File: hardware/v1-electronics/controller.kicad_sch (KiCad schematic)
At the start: 35 parts, among them IC1 IS31FL3733-QFLS4-TR, IC2 IS31FL3733-QFLS4-TR, J2 Conn_01x03, SW78 SW_Push, U1 MDBT50Q-1MV2

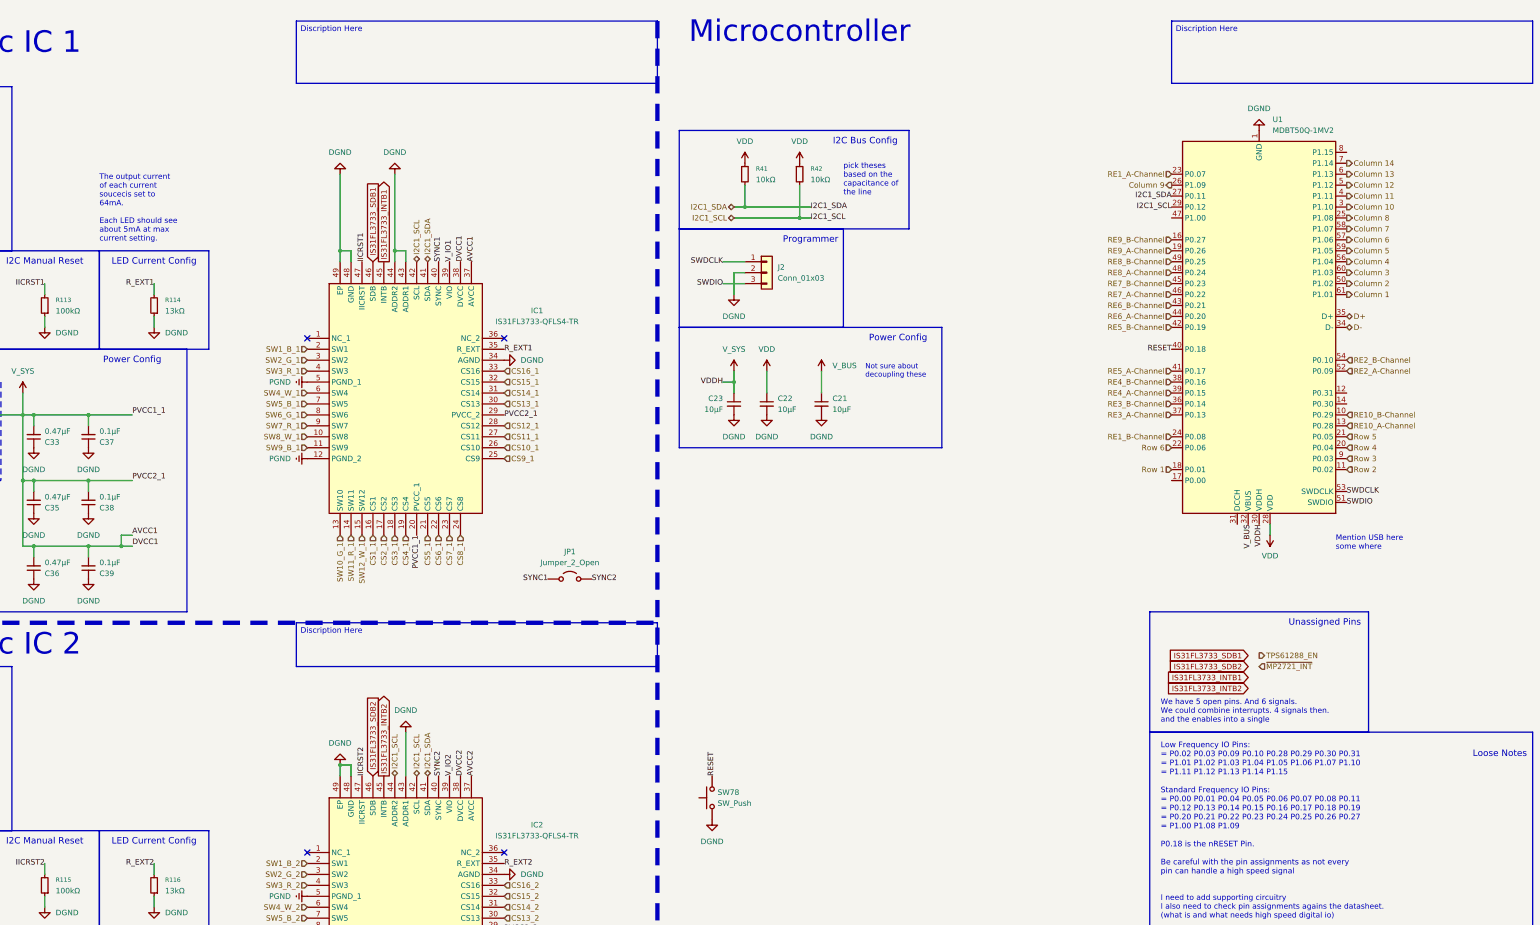
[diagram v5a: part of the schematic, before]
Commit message: refactor(v1 hardware): root level schematic is made discriptive with hierarchical pins
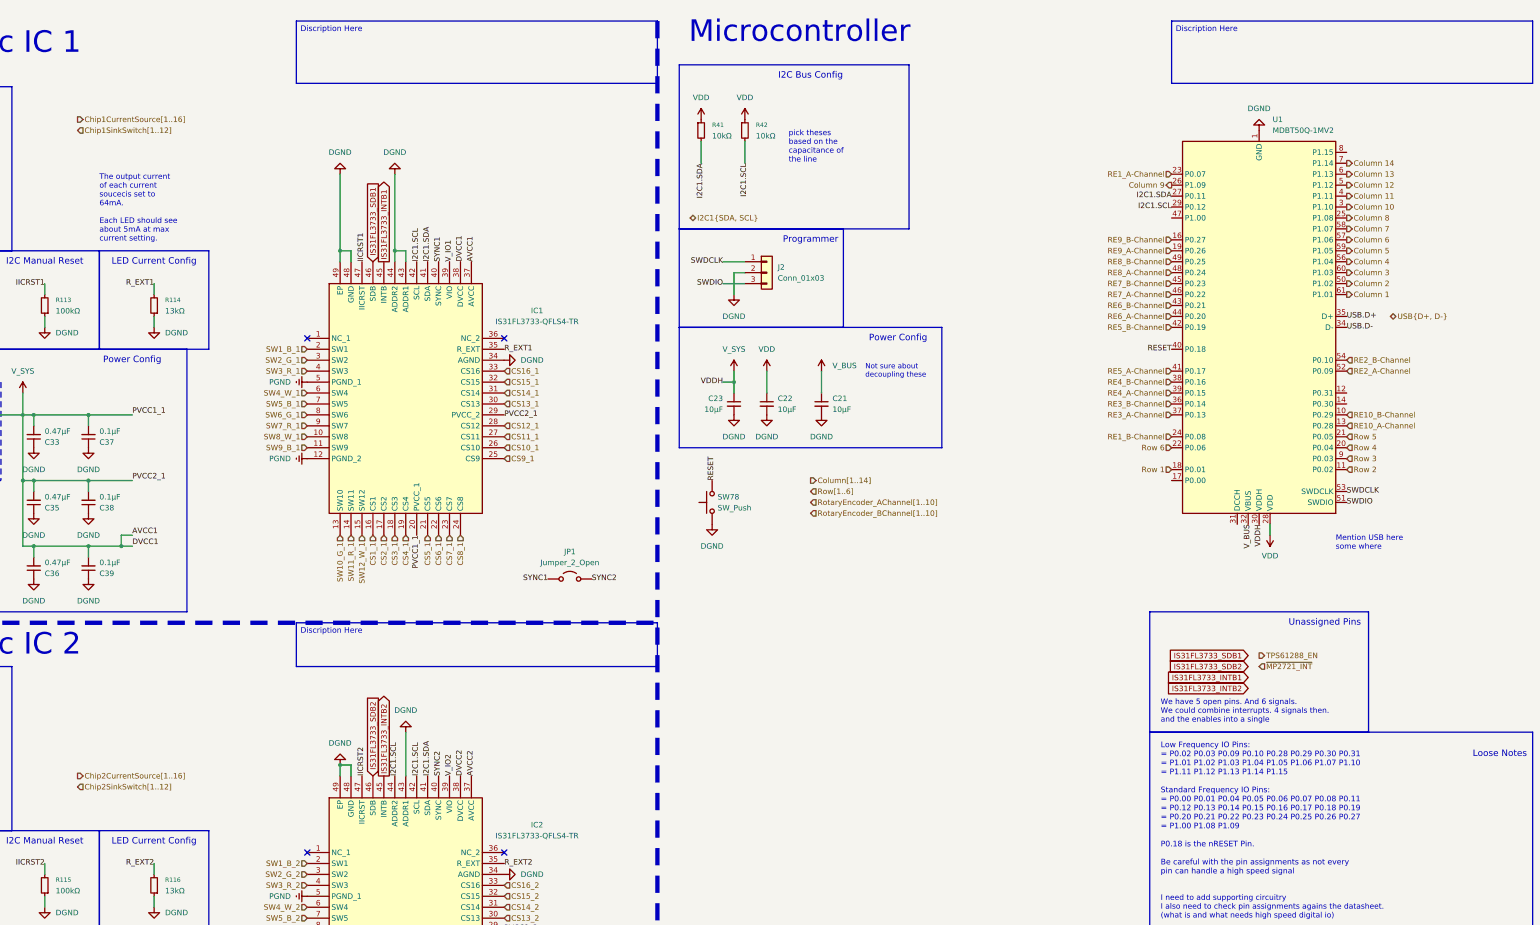
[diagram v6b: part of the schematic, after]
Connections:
- net D+ renamed USB.D+
- net D- renamed USB.D-
- net I2C1_SCL renamed I2C1.SCL
- net I2C1_SDA renamed I2C1.SDA
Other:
- moved on the sheet: R41, R42, SW78

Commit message: refactor(v1 hardware): transition to hierarchical pins complete
All the buses renamed to stuff
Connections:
- net CS10_1 renamed Chip1CurrentSource10
- net CS10_2 renamed Chip2CurrentSource10
- net CS11_1 renamed Chip1CurrentSource11
- net CS11_2 renamed Chip2CurrentSource11
- net CS12_1 renamed Chip1CurrentSource12
- net CS12_2 renamed Chip2CurrentSource12
- net CS13_1 renamed Chip1CurrentSource13
- net CS13_2 renamed Chip2CurrentSource13
- net CS14_1 renamed Chip1CurrentSource14
- net CS14_2 renamed Chip2CurrentSource14
- net CS15_1 renamed Chip1CurrentSource15
- net CS15_2 renamed Chip2CurrentSource15
- net CS16_1 renamed Chip1CurrentSource16
- net CS16_2 renamed Chip2CurrentSource16
- net CS1_1 renamed Chip1CurrentSource1
- net CS1_2 renamed Chip2CurrentSource1
- net CS2_1 renamed Chip1CurrentSource2
- net CS2_2 renamed Chip2CurrentSource2
- net CS3_1 renamed Chip1CurrentSource3
- net CS3_2 renamed Chip2CurrentSource3
- net CS4_1 renamed Chip1CurrentSource4
- net CS4_2 renamed Chip2CurrentSource4
- net CS5_1 renamed Chip1CurrentSource5
- net CS5_2 renamed Chip2CurrentSource5
- net CS6_1 renamed Chip1CurrentSource6
- net CS6_2 renamed Chip2CurrentSource6
- net CS7_1 renamed Chip1CurrentSource7
- net CS7_2 renamed Chip2CurrentSource7
- net CS8_1 renamed Chip1CurrentSource8
- net CS8_2 renamed Chip2CurrentSource8
- net CS9_1 renamed Chip1CurrentSource9
- net CS9_2 renamed Chip2CurrentSource9
- net Column 1 renamed Column1
- net Column 10 renamed Column10
- net Column 11 renamed Column11
- net Column 12 renamed Column12
- net Column 13 renamed Column13
- net Column 14 renamed Column14
- net Column 2 renamed Column2
- net Column 3 renamed Column3
- net Column 4 renamed Column4
- net Column 5 renamed Column5
- net Column 6 renamed Column6
- net Column 7 renamed Column7
- net Column 8 renamed Column8
- net Column 9 renamed Column9
- net RE10_A-Channel renamed RotaryEncoder_AChannel10
- net RE10_B-Channel renamed RotaryEncoder_BChannel10
- net RE1_A-Channel renamed RotaryEncoder_AChannel1
- net RE1_B-Channel renamed RotaryEncoder_BChannel1
- net RE2_A-Channel renamed RotaryEncoder_AChannel2
- net RE2_B-Channel renamed RotaryEncoder_BChannel2
- net RE3_A-Channel renamed RotaryEncoder_AChannel3
- net RE3_B-Channel renamed RotaryEncoder_BChannel3
- net RE4_A-Channel renamed RotaryEncoder_AChannel4
- net RE4_B-Channel renamed RotaryEncoder_BChannel4
- net RE5_A-Channel renamed RotaryEncoder_AChannel5
- net RE5_B-Channel renamed RotaryEncoder_BChannel5
- net RE6_A-Channel renamed RotaryEncoder_AChannel6
- net RE6_B-Channel renamed RotaryEncoder_BChannel6
- net RE7_A-Channel renamed RotaryEncoder_AChannel7
- net RE7_B-Channel renamed RotaryEncoder_BChannel7
- net RE8_A-Channel renamed RotaryEncoder_AChannel8
- net RE8_B-Channel renamed RotaryEncoder_BChannel8
- net RE9_A-Channel renamed RotaryEncoder_AChannel9
- net RE9_B-Channel renamed RotaryEncoder_BChannel9
- net Row 1 renamed Row1
- net Row 2 renamed Row2
- net Row 3 renamed Row3
- net Row 4 renamed Row4
- net Row 5 renamed Row5
- net Row 6 renamed Row6
- net SW10_G_1 renamed Chip1SinkSwitch10
- net SW10_G_2 renamed Chip2SinkSwitch10
- net SW11_R_1 renamed Chip1SinkSwitch11
- net SW11_R_2 renamed Chip2SinkSwitch11
- net SW12_W_1 renamed Chip1SinkSwitch12
- net SW12_W_2 renamed Chip2SinkSwitch12
- net SW1_B_1 renamed Chip1SinkSwitch1
- net SW1_B_2 renamed Chip2SinkSwitch1
- net SW2_G_1 renamed Chip1SinkSwitch2
- net SW2_G_2 renamed Chip2SinkSwitch2
- net SW3_R_1 renamed Chip1SinkSwitch3
- net SW3_R_2 renamed Chip2SinkSwitch3
- net SW4_W_1 renamed Chip1SinkSwitch4
- net SW4_W_2 renamed Chip2SinkSwitch4
- net SW5_B_1 renamed Chip1SinkSwitch5
- net SW5_B_2 renamed Chip2SinkSwitch5
- net SW6_G_1 renamed Chip1SinkSwitch6
- net SW6_G_2 renamed Chip2SinkSwitch6
- net SW7_R_1 renamed Chip1SinkSwitch7
- net SW7_R_2 renamed Chip2SinkSwitch7
- net SW8_W_1 renamed Chip1SinkSwitch8
- net SW8_W_2 renamed Chip2SinkSwitch8
- net SW9_B_1 renamed Chip1SinkSwitch9
- net SW9_B_2 renamed Chip2SinkSwitch9
- no-connect marks 4 -> 28
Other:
- note added: "Blue"
- note added: "Green"
- note added: "Red"
- note added: "White"
- moved on the sheet: IC1, JP1

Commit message: refactor(v1 hardware): refactored led controllers into a seperate sheet
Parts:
- removed C24, C26, C33, C35, C36, C40, C41, C42: 0.47μF, symbol Device:C_Small
- removed C25, C28: 22μF, symbol Device:C_Small_US
- removed C37, C38, C39, C43, C44, C45: 0.1μF, symbol Device:C_Small
- removed IC1, IC2: IS31FL3733-QFLS4-TR, QFN40P600X600X80-49N-D, symbol Lumissil Microsystems:IS31FL3733-QFLS4-TR
- removed JP1: Jumper_2_Open, symbol Jumper:Jumper_2_Open
- removed R102, R103, R104, R105, R113, R115: 100kΩ, symbol Device:R_Small
- removed R114, R116: 13kΩ, symbol Device:R_Small
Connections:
- no-connect marks 28 -> 0
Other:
- note removed: "Blue"
- note removed: "Green"
- note removed: "High Current Noise Reduction"
- note removed: "I2C IO Config"
- note removed: "I2C Manual Reset"
- note removed: "LED Current Config"
- note removed: "LED Matric IC 1"
- note removed: "LED Matric IC 2"
- note removed: "Red"
- note removed: "Signal Config"
- note removed: "The output current of each current soucecis set to 64mA. Each LED should see about 5mA at max current setting."
- note removed: "White"
- moved on the sheet: C21, C22, C23, J2, R41, R42, SW78, U1
